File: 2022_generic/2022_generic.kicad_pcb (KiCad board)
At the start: 2 copper layers, 50.8 x 43.2 mm, 18 parts, among them J1 Screw_Terminal_01x02, J2 Programming Connector, SW1 6mm tactile button, U1 PIC16LF15313

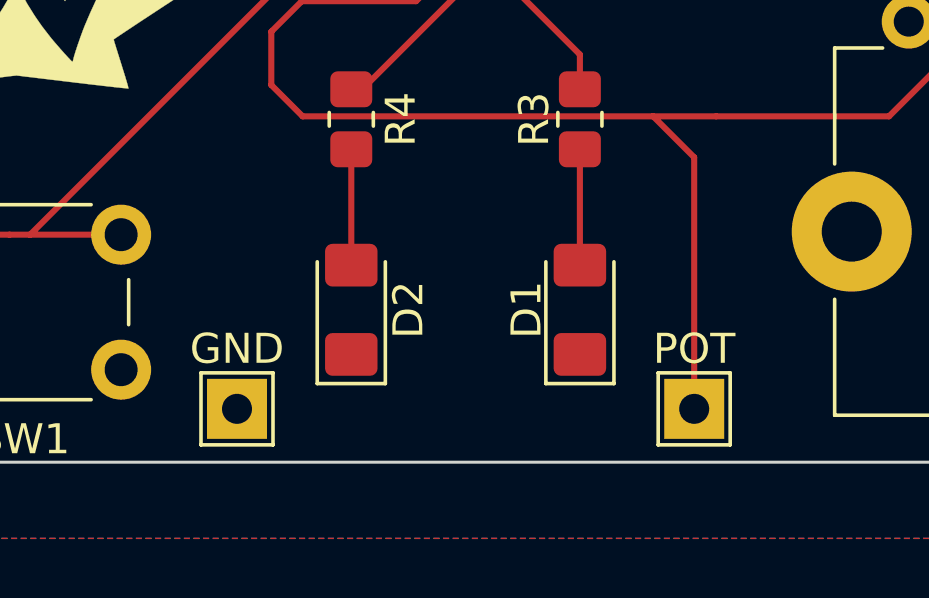
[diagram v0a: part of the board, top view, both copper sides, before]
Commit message: Add pot explanation and test point numbers
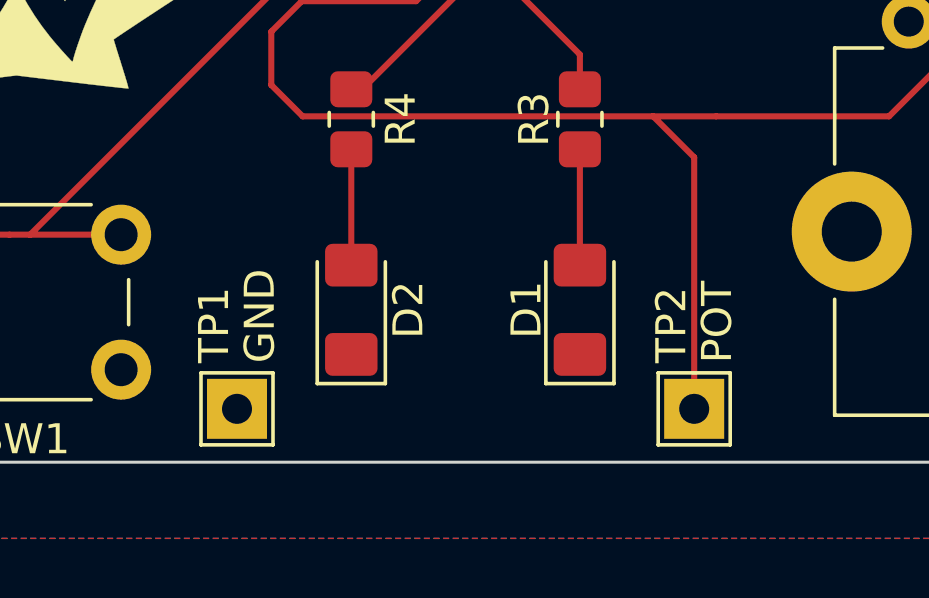
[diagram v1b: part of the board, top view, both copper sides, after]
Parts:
- renumbered GND to TP1, POT to TP2
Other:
- board text added: "POT"
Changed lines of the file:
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@@
     (property "Sheetname" "")
     (attr exclude_from_pos_files)
-    (fp_text reference "POT" (at 0 -1.998) (layer "F.SilkS")
-      (effects (font (size 1 1) (thickness 0.15)))
+    (fp_text reference "TP2" (at -0.762 -1.524 90) (layer "F.SilkS")
+      (effects (font (size 1 1) (thickness 0.15)) (justify left))
     )
     (fp_text value "TestPoint" (at 0 2.05) (layer "F.Fab")
@@
     (property "Sheetname" "")
     (attr exclude_from_pos_files)
-    (fp_text reference "GND" (at 0 -1.998) (layer "F.SilkS")
-      (effects (font (size 1 1) (thickness 0.15)))
+    (fp_text reference "TP1" (at -0.762 -1.524 90) (layer "F.SilkS")
+      (effects (font (size 1 1) (thickness 0.15)) (justify left))
     )
     (fp_text value "TestPoint" (at 0 2.05) (layer "F.Fab")
@@
     (effects (font (size 1.3 1.3) (thickness 0.2)) (justify mirror))
   )
+  (gr_text "GND" (at 151.892 136.398 90) (layer "F.SilkS")
+    (effects (font (size 1 1) (thickness 0.15)) (justify left))
+  )
   (gr_text "GND" (at 141.478 100.076) (layer "F.SilkS")
     (effects (font (size 1.5 1.5) (thickness 0.375)))
@@
     (effects (font (size 1.5 1.5) (thickness 0.375)))
   )
+  (gr_text "POT" (at 167.132 136.398 90) (layer "F.SilkS")
+    (effects (font (size 1 1) (thickness 0.15)) (justify left))
+  )
   (segment (start 168.132 114.554) (end 173.436784 109.249216) (width 0.2032) (layer "F.Cu") (net 1))
